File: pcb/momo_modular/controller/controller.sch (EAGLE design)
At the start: 19 parts, among them U6 PIC24F16KA101-X_PSSOP, U7 FLASH8MSOP8

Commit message: Finished version 1 of the controller and wall_power boards.
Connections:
- removed net RX: U6.U1RX/U1BCLK/CN6/RB2
- removed net TX: U6.U1TX/INT0/CN23/RB7
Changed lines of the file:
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@@
 <setting verticaltext="up"/>
 </settings>
-<grid distance="0.05" unitdist="inch" unit="inch" style="lines" multiple="1" display="no" altdistance="0.01" altunitdist="inch" altunit="inch"/>
+<grid distance="0.1" unitdist="inch" unit="inch" style="lines" multiple="1" display="no" altdistance="0.01" altunitdist="inch" altunit="inch"/>
 <layers>
 <layer number="1" name="Top" color="4" fill="1" visible="no" active="no"/>
@@
 </segment>
 </net>
-<net name="RX" class="0">
-<segment>
-<pinref part="U6" gate="A" pin="U1RX/U1BCLK/CN6/RB2"/>
-<wire x1="-193.04" y1="-2.54" x2="-203.2" y2="-2.54" width="0.1524" layer="91"/>
-<label x="-198.12" y="-2.54" size="1.778" layer="95"/>
-</segment>
-</net>
-<net name="TX" class="0">
-<segment>
-<pinref part="U6" gate="A" pin="U1TX/INT0/CN23/RB7"/>
-<wire x1="-193.04" y1="-5.08" x2="-203.2" y2="-5.08" width="0.1524" layer="91"/>
-<label x="-198.12" y="-5.08" size="1.778" layer="95"/>
-</segment>
-</net>

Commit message: Controller Board v2.1 Done
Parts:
- removed U$2: 2X3-MOLEX-90130, components:2X3-MOLEX-90130
- removed U$4: MOMO-EDGE-SMALL-F, components:MOMO-EDGE-SMALL-F
- added JP1: (no value), pinhead:PINHD-1X5
- U$1: value MOMO-EDGE-POWER-F -> MOMO-EDGE-8F; device components:MOMO-EDGE-POWER-F -> components:MOMO-EDGE-8F
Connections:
- removed net N$18: U$2.3, U6.PGC1/AN3/C1INC/C2INA/U2RX/U2BCLK/CN5/RB1
- removed net N$19: U$2.4, U6.PGD1/AN2/C1IND/C2INB/U2TX/CN4/RB0
- new net N$6: JP1.4, U6.PGD1/AN2/C1IND/C2INB/U2TX/CN4/RB0
- new net N$7: JP1.5, U6.PGC1/AN3/C1INC/C2INA/U2RX/U2BCLK/CN5/RB1
- net GND: now also JP1.3, U$1.PGND; no longer U$2.6, U$4.GND
- net ICLK: now also U$1.CLK; no longer U$4.SCL
- net IDAT: now also U$1.DAT; no longer U$4.SDA
- net IRQ: now also U$1.ALRM; no longer U$4.IRQ
- net N$15: now also JP1.1; no longer U$2.5
- net V+: now also U$1.4V; no longer U$1.3.8V, U$2.2
- net VCCINT: now also U$1.2.8V; no longer U$2.1, U$4.2.8V
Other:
- note removed: "Board Connector"

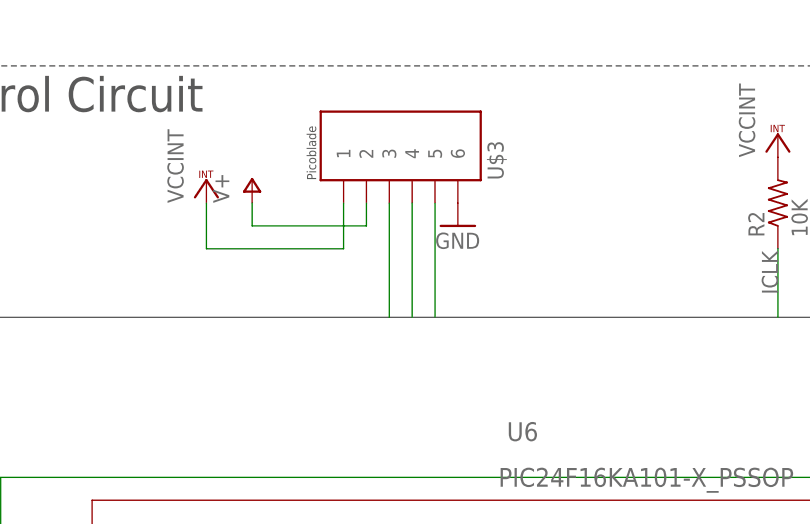
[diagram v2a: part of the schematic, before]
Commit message: Updated MoMo FSU to version 2.  Following major changes: 1. Removed unneeded header for momo programming. 2. Removed mux and analog switches allowing serial passthrough, all communication with momo will be over mib. 3. standardized momo connector 4. relaid out board
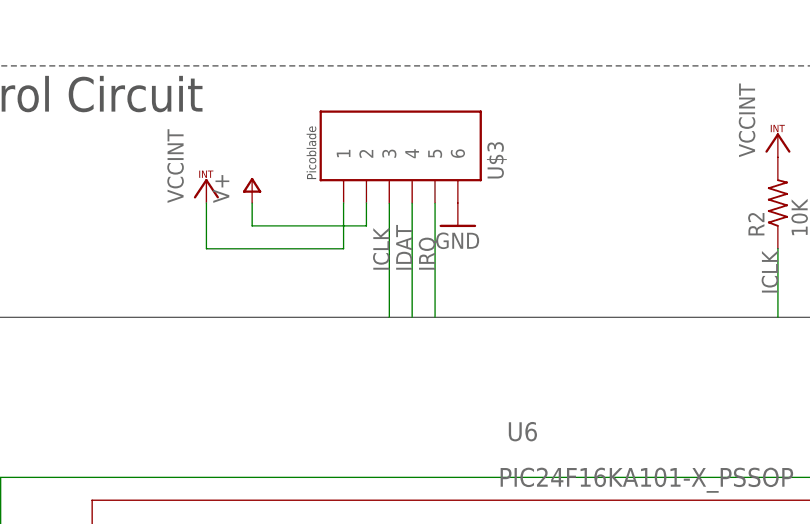
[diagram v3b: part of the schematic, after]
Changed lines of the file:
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@@
 <pinref part="U$3" gate="G$1" pin="5"/>
 <wire x1="-149.86" y1="38.1" x2="-149.86" y2="50.8" width="0.1524" layer="91"/>
+<label x="-149.86" y="43.18" size="1.778" layer="95" rot="R90"/>
 </segment>
 <segment>
@@
 <pinref part="U$3" gate="G$1" pin="4"/>
 <wire x1="-152.4" y1="38.1" x2="-152.4" y2="50.8" width="0.1524" layer="91"/>
+<label x="-152.4" y="43.18" size="1.778" layer="95" rot="R90"/>
 </segment>
 <segment>
@@
 <pinref part="U$3" gate="G$1" pin="3"/>
 <wire x1="-154.94" y1="38.1" x2="-154.94" y2="50.8" width="0.1524" layer="91"/>
+<label x="-154.94" y="43.18" size="1.778" layer="95" rot="R90"/>
 </segment>
 <segment>
